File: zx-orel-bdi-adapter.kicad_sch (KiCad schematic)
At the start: 26 parts, among them J1 Barrel_Jack_Switch, J2 DB9_Male, J3 Conn_02x32_Row_Letter_First, J4 Conn_02x03_Odd_Even, J5 Conn_02x03_Odd_Even, Q1 BC558, Q2 BC558, SW1 SW_Push_Dual, U1 74LS30, U2 74LS27, U4 74LS640, U5 28C256, U6 74LS32

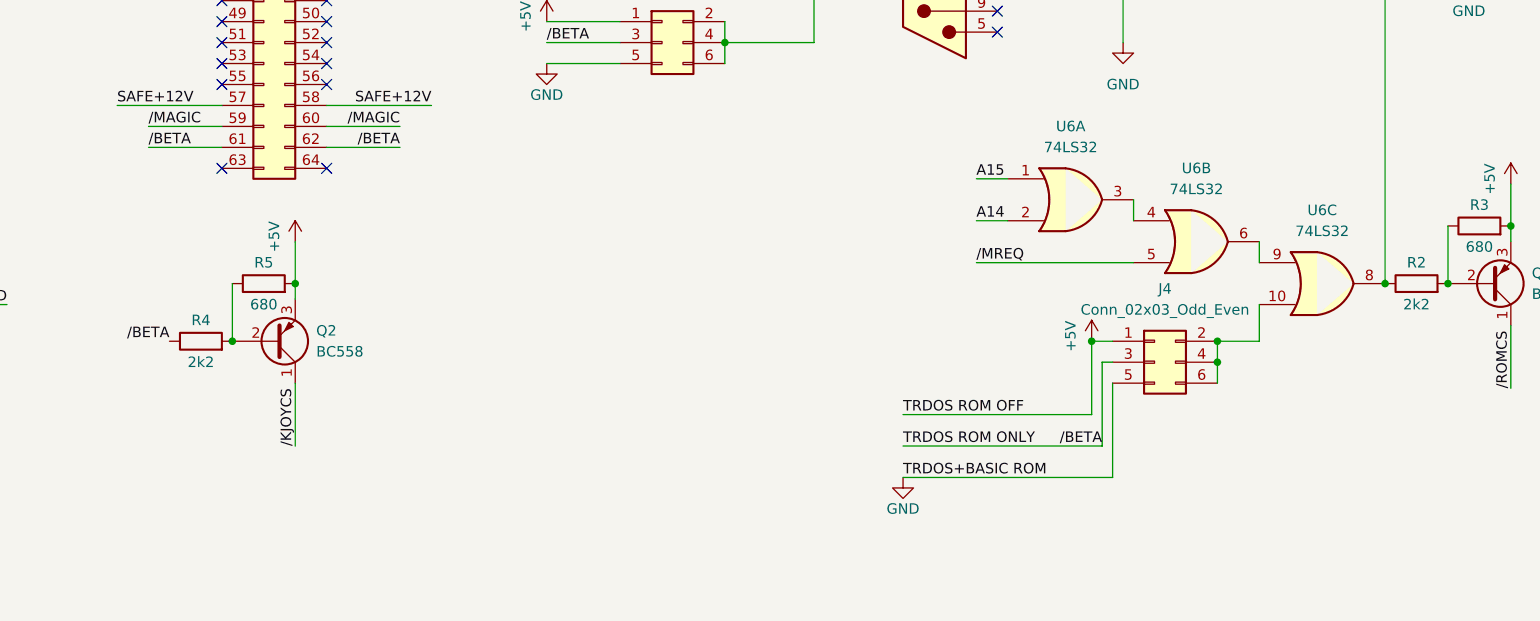
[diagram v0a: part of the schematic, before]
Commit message: fixed BETA and /BETA output usage to block TRDOS only and re-routed pcb
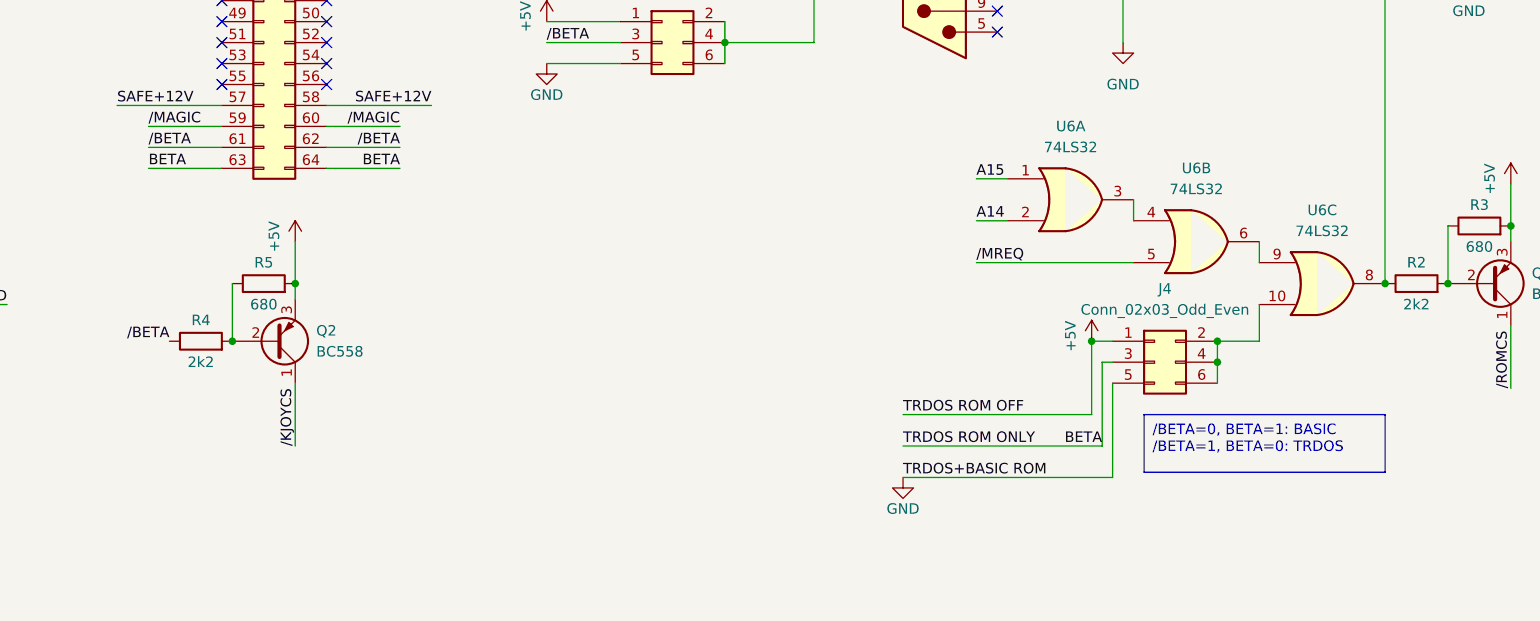
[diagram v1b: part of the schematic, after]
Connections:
- net BETA: now reaches J3.63 (Pin_63)
- net BETA: now also J3.64 (Pin_64), J4.3 (Pin_3)
- net TRDOS ROM ONLY renamed /BETA
- net /BETA: no longer J4.3 (Pin_3)
- no-connect marks 50 -> 48
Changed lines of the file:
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@@
   (no_connect (at 154.305 184.785))
   (no_connect (at 129.54 74.93))
-  (no_connect (at 116.84 97.79))
   (no_connect (at 133.985 187.325))
   (no_connect (at 210.82 78.74))
@@
   (no_connect (at 116.84 85.09))
   (no_connect (at 129.54 85.09))
-  (no_connect (at 129.54 97.79))
   (no_connect (at 44.45 73.66))
   (no_connect (at 116.84 82.55))
@@
     (stroke (width 0) (type default))
   )
+  (wire (pts (xy 107.95 97.79) (xy 116.84 97.79))
+    (stroke (width 0) (type default))
+  )
   (wire (pts (xy 182.88 25.4) (xy 189.23 25.4))
     (stroke (width 0) (type default))
@@
     (stroke (width 0) (type default))
   )
+  (wire (pts (xy 129.54 97.79) (xy 138.43 97.79))
+    (stroke (width 0) (type default))
+  )
   (wire (pts (xy 220.98 66.04) (xy 220.98 35.56))
     (stroke (width 0) (type default))
@@
     (stroke (width 0) (type default))
   )
+  (text_box "/BETA=0, BETA=1: BASIC\n/BETA=1, BETA=0: TRDOS"
+    (at 228.6 127.635 0) (size 29.21 6.985)
+    (stroke (width 0) (type default))
+    (fill (type none))
+    (effects (font (size 1.27 1.27)) (justify left top))
+  )
   (label "A02" (at 138.43 52.07 180) (fields_autoplaced)
     (effects (font (size 1.27 1.27)) (justify right bottom))
@@
     (effects (font (size 1.27 1.27)) (justify left bottom))
   )
-  (label "{slash}BETA" (at 223.52 131.445 180) (fields_autoplaced)
+  (label "BETA" (at 223.52 131.445 180) (fields_autoplaced)
     (effects (font (size 1.27 1.27)) (justify right bottom))
   )
@@
     (effects (font (size 1.27 1.27)) (justify right bottom))
   )
+  (label "BETA" (at 138.43 97.79 180) (fields_autoplaced)
+    (effects (font (size 1.27 1.27)) (justify right bottom))
+  )
   (label "D2" (at 189.23 35.56 0) (fields_autoplaced)
     (effects (font (size 1.27 1.27)) (justify left bottom))
@@
     (effects (font (size 1.27 1.27)) (justify left bottom))
   )
+  (label "BETA" (at 107.95 97.79 0) (fields_autoplaced)
+    (effects (font (size 1.27 1.27)) (justify left bottom))
+  )

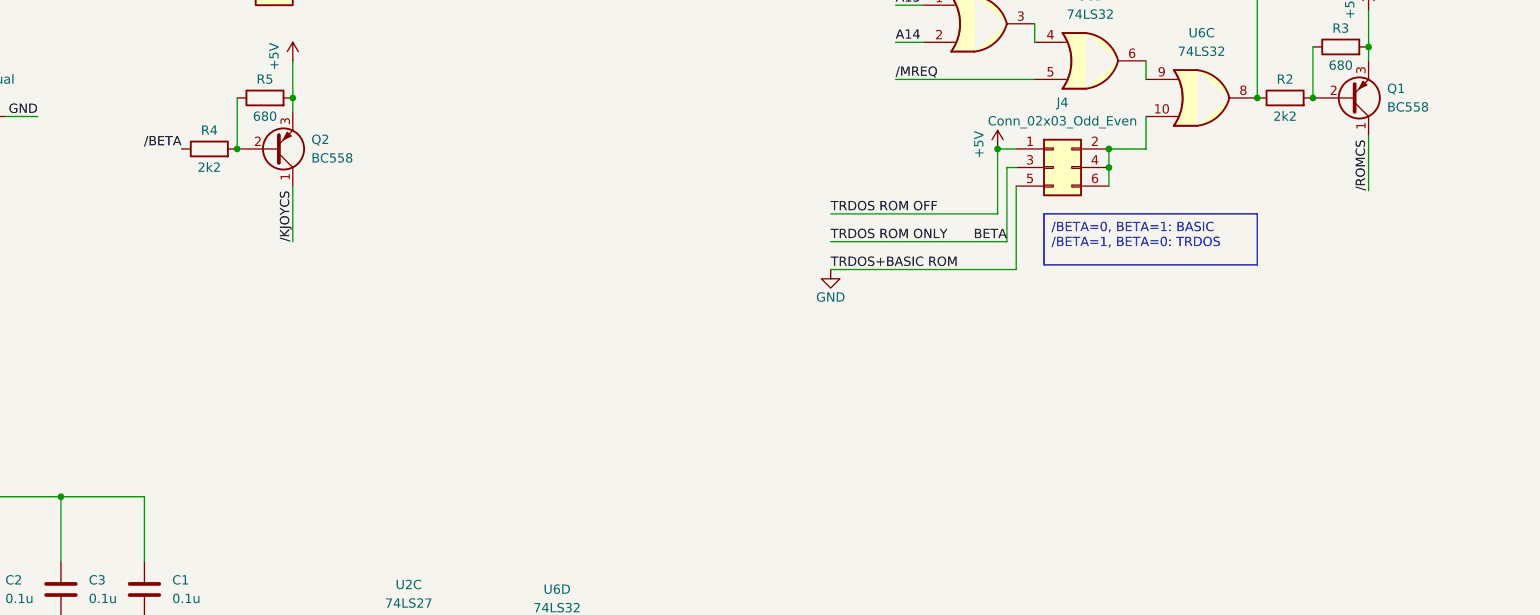
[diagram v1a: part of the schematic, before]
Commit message: Fixed bug with flipped TRDOS signal
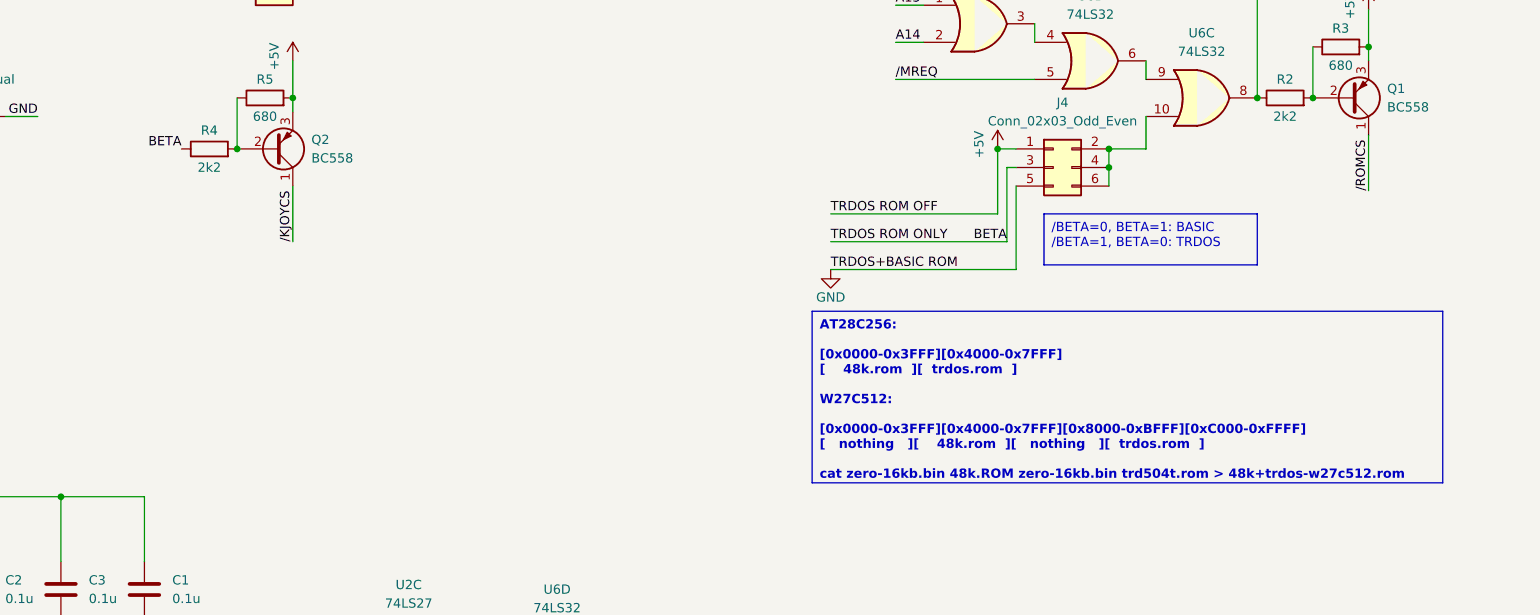
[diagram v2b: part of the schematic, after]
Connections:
- net BETA: now also R4.1
- net /BETA: no longer R4.1
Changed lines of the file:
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@@
     (effects (font (size 1.27 1.27)) (justify left top))
+  )
+  (text_box "AT28C256:\n\n[0x0000-0x3FFF][0x4000-0x7FFF]\n[    48k.rom  ][  trdos.rom  ]\n\nW27C512:\n\n[0x0000-0x3FFF][0x4000-0x7FFF][0x8000-0xBFFF][0xC000-0xFFFF]\n[   nothing   ][    48k.rom  ][   nothing   ][  trdos.rom  ]\n\ncat zero-16kb.bin 48k.ROM zero-16kb.bin trd504t.rom > 48k+trdos-w27c512.rom"
+    (at 196.85 140.97 0) (size 86.36 23.495)
+    (stroke (width 0) (type default))
+    (fill (type none))
+    (effects (font (size 1.27 1.27) (thickness 0.254) bold) (justify left top))
   )
   (label "A02" (at 138.43 52.07 180) (fields_autoplaced)
@@
     (effects (font (size 1.27 1.27)) (justify left bottom))
   )
-  (label "{slash}BETA" (at 110.49 118.745 180) (fields_autoplaced)
+  (label "BETA" (at 110.49 118.745 180) (fields_autoplaced)
     (effects (font (size 1.27 1.27)) (justify right bottom))
   )
